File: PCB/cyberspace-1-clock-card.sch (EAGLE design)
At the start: 40 parts, among them U1 555, U2 Quad AND Gate, U3 Quad AND Gate, U4 QUAD NAND Gate, U5 SCHMIDT INVERTER, U6 HCT32, X1 1-14MHz

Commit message: Clock Card final?
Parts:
- added LOGO1: (no value), gfx-glyphs:SOZU-BRAND-LOGO-20MM
- added LOGO2: (no value), gfx-glyphs:CHRONOS-LOGO-20MM
- R13: value 1K -> 2K
- U2, U3: value Quad AND Gate -> HCT08
- U4: value QUAD NAND Gate -> HCT00
- U5: value SCHMIDT INVERTER -> HCT14
- renumbered RP1 to SLOW_ADJ
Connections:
- net !CLK_OUT: now also R13.1; no longer CLK.C
- net N$11: now also CLK.C, R13.2; no longer CLK.A, R13.1
- net VCC: now also CLK.A; no longer R13.2
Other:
- moved on the sheet: CLK, L_FAST, L_MAN, L_SLOW, PCB, R13, R4, R5, R6, U2.1, U2.2, U2.3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

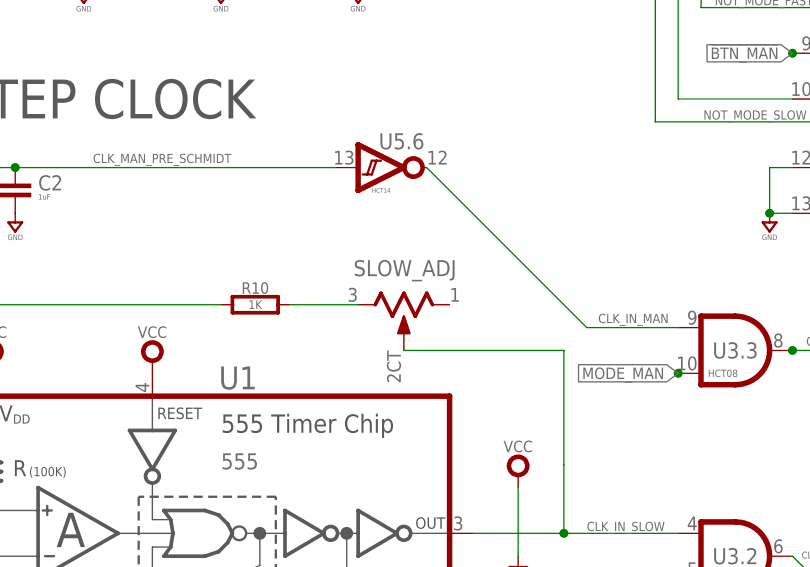
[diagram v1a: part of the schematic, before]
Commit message: Resistor missing value.
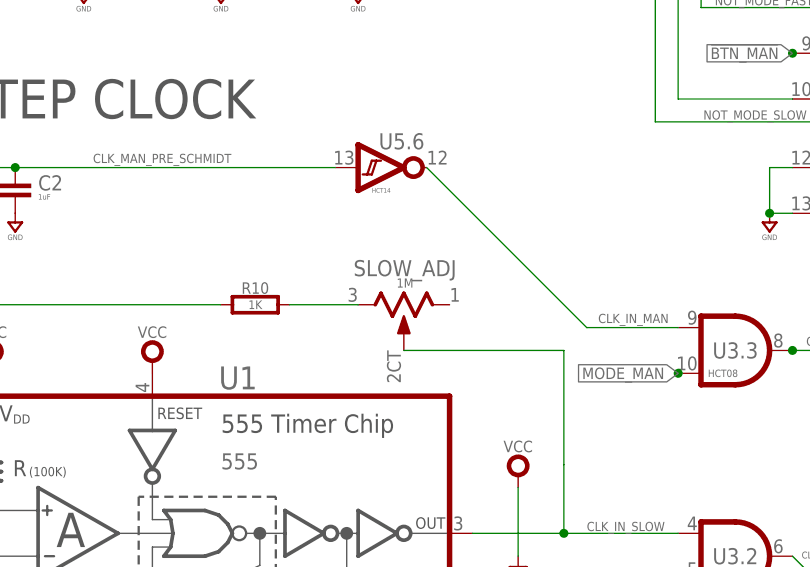
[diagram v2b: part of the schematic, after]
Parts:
- SLOW_ADJ: value (none) -> 1M
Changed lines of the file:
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@@
 <part name="SUPPLY43" library="supply" library_urn="urn:adsk.eagle:library:10485988" deviceset="VCC" device=""/>
 <part name="SUPPLY44" library="supply" library_urn="urn:adsk.eagle:library:10485988" deviceset="GND" device=""/>
-<part name="SLOW_ADJ" library="rlc" library_urn="urn:adsk.eagle:library:4192893" deviceset="CERMET_MULTI_TURN" device="-3006P" package3d_urn="urn:adsk.eagle:package:42461647/1"/>
+<part name="SLOW_ADJ" library="rlc" library_urn="urn:adsk.eagle:library:4192893" deviceset="CERMET_MULTI_TURN" device="-3006P" package3d_urn="urn:adsk.eagle:package:42461647/1" value="1M"/>
 <part name="CLK" library="led" library_urn="urn:adsk.eagle:library:5499911" deviceset="SMT" device="0603" package3d_urn="urn:adsk.eagle:package:5499947/3"/>
 <part name="R13" library="rlc" library_urn="urn:adsk.eagle:library:4192893" deviceset="RESISTOR" device="0603" package3d_urn="urn:adsk.eagle:package:4193040/5" value="2K"/>

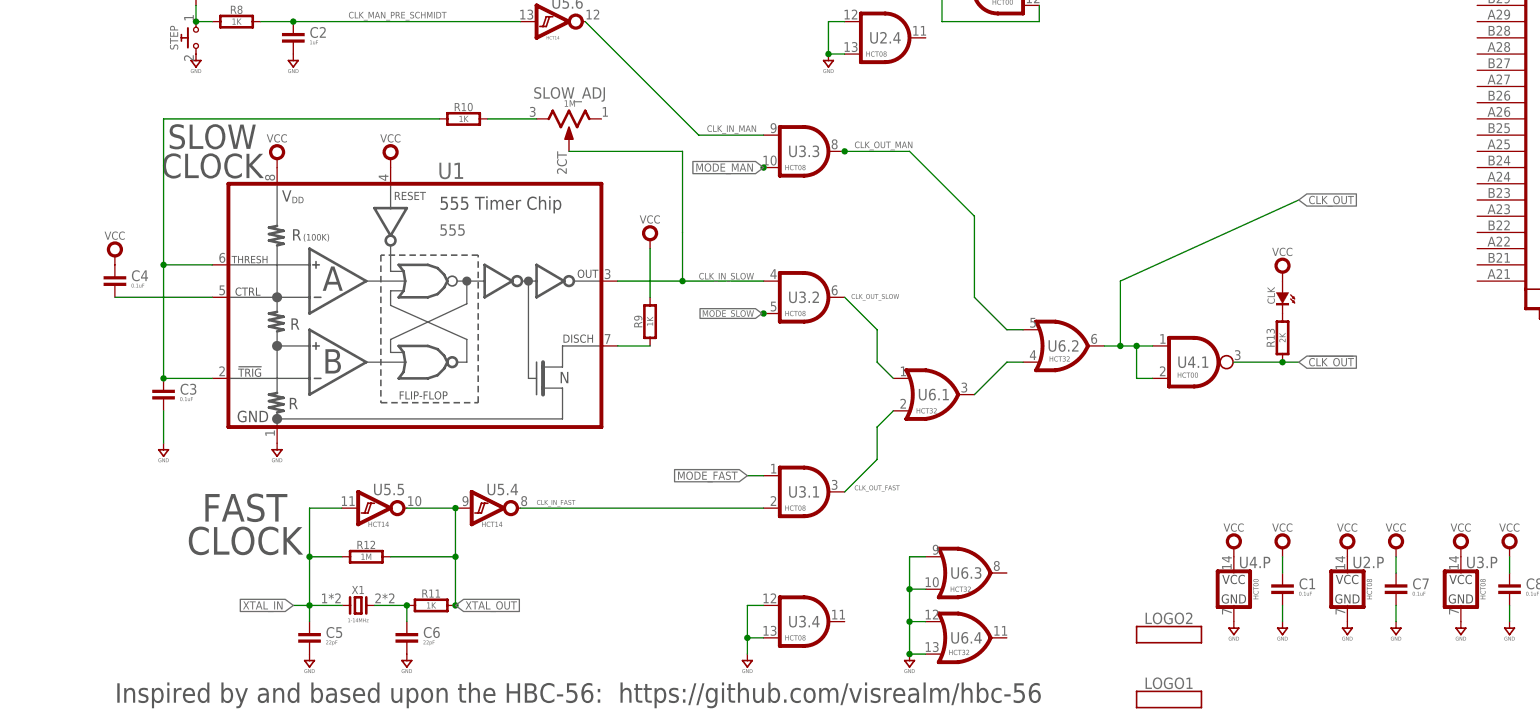
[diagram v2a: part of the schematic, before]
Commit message: WIP. Proposed clock fix in schematic.
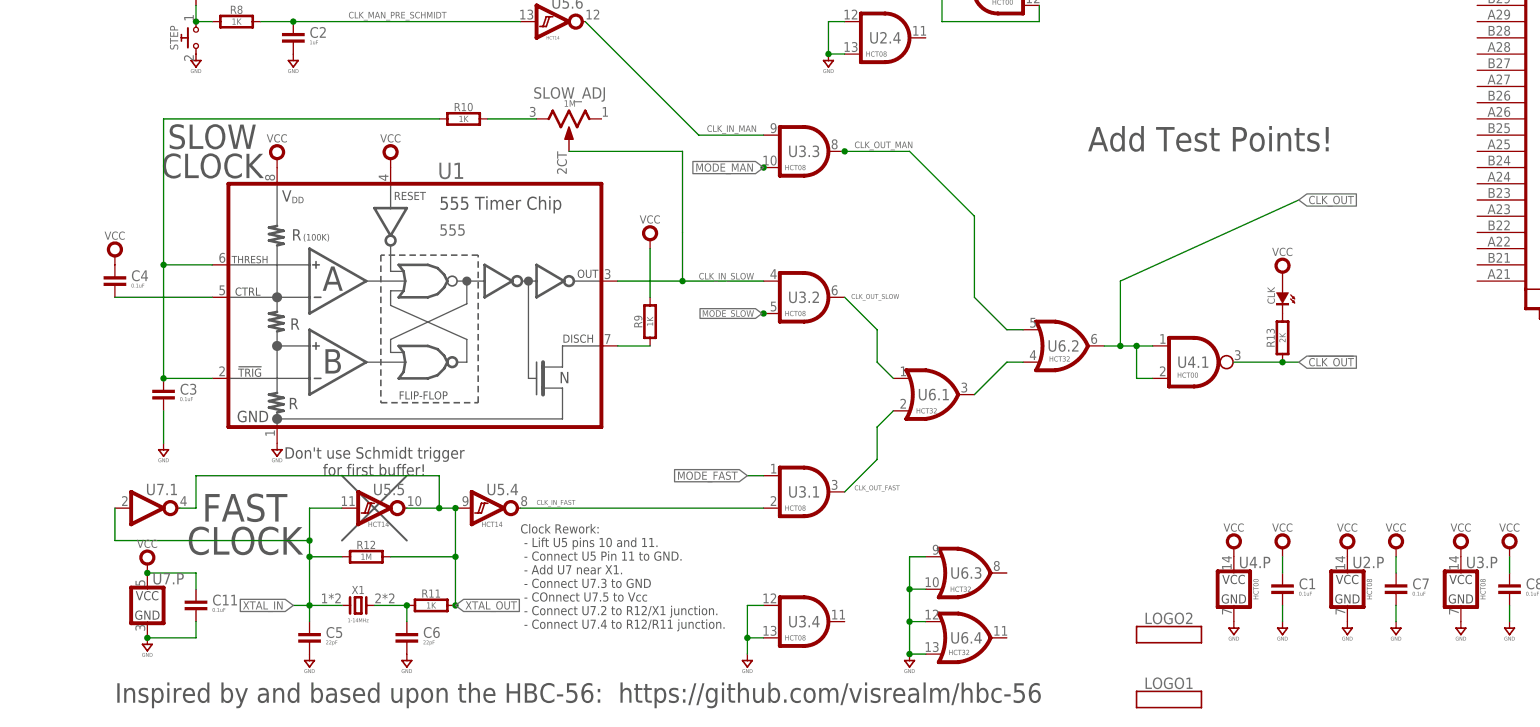
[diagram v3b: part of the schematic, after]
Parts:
- added C11: 0.1uF, rlc:CAPACITOR0603
- added U7: (no value), logic:74HCT1G-TSOP504
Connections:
- net GND: now also C11.2, U7.P.GND
- net VCC: now also C11.1, U7.P.VCC
- net XTAL_IN: now also U7.1.A
- net XTAL_OUT: now also U7.1.Y
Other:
- note added: "Add Test Points!"
- note added: "Clock Rework: - Lift U5 pins 10 and 11. - Connect U5 Pin 11 to GND. - Add U7 near X1. - Connect U7.3 to GND - COnnect U7.5 to Vcc - Connect U7.2 to R12/X1 junction. - Connect U7.4 to R12/R11 junction."
- note added: "Don't use Schmidt trigger for first buffer!"
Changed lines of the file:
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@@
 <part name="SUPPLY46" library="supply" library_urn="urn:adsk.eagle:library:10485988" deviceset="GND" device=""/>
 <part name="U$1" library="frames-custom" library_urn="urn:adsk.eagle:library:11820551" deviceset="DINA4_L-SMALLDOC" device="">
-<attribute name="REV" value="A"/>
+<attribute name="REV" value="B"/>
 </part>
 <part name="LOGO1" library="gfx-glyphs" library_urn="urn:adsk.eagle:library:17868973" deviceset="SOZU-BRAND-LOGO" device="-20MM"/>
 <part name="LOGO2" library="gfx-glyphs" library_urn="urn:adsk.eagle:library:17868973" deviceset="CHRONOS-LOGO" device="-20MM"/>
+<part name="U7" library="logic" library_urn="urn:adsk.eagle:library:8032508" deviceset="74*1G?04" device="-TSOP5" package3d_urn="urn:adsk.eagle:package:8032592/3" technology="HCT"/>
+<part name="SUPPLY47" library="supply" library_urn="urn:adsk.eagle:library:10485988" deviceset="GND" device=""/>
+<part name="SUPPLY48" library="supply" library_urn="urn:adsk.eagle:library:10485988" deviceset="VCC" device=""/>
+<part name="C11" library="rlc" library_urn="urn:adsk.eagle:library:4192893" deviceset="CAPACITOR" device="0603" package3d_urn="urn:adsk.eagle:package:4193021/5" value="0.1uF"/>
 </parts>
 <sheets>
@@
 <text x="40.64" y="116.84" size="4.318" layer="97" ratio="15" distance="20" align="center">STEP CLOCK</text>
 <text x="55.88" y="157.48" size="4.318" layer="97" ratio="15" distance="20" align="center">CLOCK MODE SELECT</text>
+<text x="154.94" y="88.9" size="3.81" layer="97">Add Test Points!</text>
+<text x="43.18" y="38.1" size="1.778" layer="97" align="bottom-center">Don't use Schmidt trigger
+for first buffer!</text>
+<wire x1="48.26" y1="27.94" x2="38.1" y2="38.1" width="0.3048" layer="97"/>
+<wire x1="38.1" y1="27.94" x2="48.26" y2="38.1" width="0.3048" layer="97"/>
+<text x="66.04" y="30.48" size="1.4224" layer="97" align="top-left">Clock Rework:
+ - Lift U5 pins 10 and 11.
+ - Connect U5 Pin 11 to GND.
+ - Add U7 near X1.
+ - Connect U7.3 to GND
+ - COnnect U7.5 to Vcc
+ - Connect U7.2 to R12/X1 junction.
+ - Connect U7.4 to R12/R11 junction.</text>
 </plain>
 <instances>
@@
 <attribute name="NAME" x="167.64" y="15.748" size="1.778" layer="95" font="vector" ratio="15" align="center"/>
 <attribute name="VALUE" x="167.64" y="13.208" size="1.016" layer="96" font="vector" align="center"/>
+</instance>
+<instance part="U7" gate=".1" x="7.62" y="33.02" smashed="yes">
+<attribute name="NAME" x="7.366" y="35.052" size="1.778" layer="95" ratio="15"/>
+<attribute name="VALUE" x="6.604" y="30.48" size="0.8128" layer="95" font="vector" align="center-left"/>
+</instance>
+<instance part="U7" gate=".P" x="7.62" y="17.78" smashed="yes">
+<attribute name="NAME" x="8.382" y="21.082" size="1.778" layer="95" font="vector" ratio="15"/>
+<attribute name="VALUE" x="10.668" y="17.78" size="0.8128" layer="96" font="vector" rot="R90" align="top-center"/>
+</instance>
+<instance part="SUPPLY47" gate="GND" x="7.62" y="12.7" smashed="yes">
+<attribute name="VALUE" x="7.62" y="10.033" size="0.6096" layer="96" font="vector" align="center"/>
+</instance>
+<instance part="SUPPLY48" gate="G$1" x="7.62" y="22.86" smashed="yes">
+<attribute name="VALUE" x="7.62" y="26.797" size="1.27" layer="96" font="vector" ratio="15" align="bottom-center"/>
+</instance>
+<instance part="C11" gate="G$1" x="15.24" y="17.78" smashed="yes">
+<attribute name="NAME" x="17.78" y="17.78" size="1.6764" layer="95" font="vector" ratio="15"/>
+<attribute name="VALUE" x="17.78" y="16.764" size="0.6096" layer="96" font="vector"/>
 </instance>
 </instances>
@@
 <pinref part="SUPPLY46" gate="GND" pin="GND"/>
 </segment>
+<segment>
+<pinref part="U7" gate=".P" pin="GND"/>
+<pinref part="SUPPLY47" gate="GND" pin="GND"/>
+<pinref part="C11" gate="G$1" pin="2"/>
+<wire x1="15.24" y1="15.24" x2="15.24" y2="12.7" width="0.1524" layer="91"/>
+<wire x1="15.24" y1="12.7" x2="7.62" y2="12.7" width="0.1524" layer="91"/>
+<junction x="7.62" y="12.7"/>
+</segment>
 </net>
 <net name="VCC" class="0">
@@
 <pinref part="CLK" gate="G$1" pin="A"/>
 <pinref part="SUPPLY21" gate="G$1" pin="VCC"/>
+</segment>
+<segment>
+<pinref part="U7" gate=".P" pin="VCC"/>
+<pinref part="SUPPLY48" gate="G$1" pin="VCC"/>
+<wire x1="7.62" y1="22.86" x2="15.24" y2="22.86" width="0.1524" layer="91"/>
+<junction x="7.62" y="22.86"/>
+<pinref part="C11" gate="G$1" pin="1"/>
+<wire x1="15.24" y1="22.86" x2="15.24" y2="20.32" width="0.1524" layer="91"/>
 </segment>
 </net>
@@
 <wire x1="33.02" y1="17.78" x2="33.02" y2="15.24" width="0.1524" layer="91"/>
 <label x="30.48" y="17.78" size="1.27" layer="95" rot="R180" xref="yes"/>
-<wire x1="33.02" y1="25.4" x2="33.02" y2="33.02" width="0.1524" layer="91"/>
+<wire x1="33.02" y1="25.4" x2="33.02" y2="27.94" width="0.1524" layer="91"/>
 <junction x="33.02" y="25.4"/>
 <pinref part="U5" gate=".5" pin="A"/>
+<wire x1="33.02" y1="27.94" x2="33.02" y2="33.02" width="0.1524" layer="91"/>
 <wire x1="33.02" y1="33.02" x2="38.1" y2="33.02" width="0.1524" layer="91"/>
+<wire x1="33.02" y1="27.94" x2="2.54" y2="27.94" width="0.1524" layer="91"/>
+<junction x="33.02" y="27.94"/>
+<pinref part="U7" gate=".1" pin="A"/>
+<wire x1="2.54" y1="27.94" x2="2.54" y2="33.02" width="0.1524" layer="91"/>
 </segment>
 </net>
@@
 <pinref part="U5" gate=".5" pin="Y"/>
 <pinref part="U5" gate=".4" pin="A"/>
-<wire x1="48.26" y1="33.02" x2="55.88" y2="33.02" width="0.1524" layer="91"/>
+<wire x1="48.26" y1="33.02" x2="53.34" y2="33.02" width="0.1524" layer="91"/>
+<wire x1="53.34" y1="33.02" x2="55.88" y2="33.02" width="0.1524" layer="91"/>
 <wire x1="55.88" y1="25.4" x2="55.88" y2="33.02" width="0.1524" layer="91"/>
 <junction x="55.88" y="25.4"/>
 <junction x="55.88" y="33.02"/>
+<wire x1="53.34" y1="33.02" x2="53.34" y2="38.1" width="0.1524" layer="91"/>
+<junction x="53.34" y="33.02"/>
+<wire x1="53.34" y1="38.1" x2="15.24" y2="38.1" width="0.1524" layer="91"/>
+<wire x1="15.24" y1="38.1" x2="15.24" y2="33.02" width="0.1524" layer="91"/>
+<pinref part="U7" gate=".1" pin="Y"/>
+<wire x1="15.24" y1="33.02" x2="12.7" y2="33.02" width="0.1524" layer="91"/>
 </segment>
 </net>
